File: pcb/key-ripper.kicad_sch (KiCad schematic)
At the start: 193 parts, among them J1 Conn_01x03, SW1 ESC, SW10 F9, SW11 F10, SW12 F11, SW13 F12, SW14 TILDE, SW15 1, SW16 2, SW17 3, SW18 4, SW19 5, SW2 F1, SW20 6, SW21 7, SW22 8, SW23 9, SW24 0, SW25 -, SW26 +, SW27 BACKSPACE, SW28 TAB, SW29 Q, SW3 F2, SW30 W, SW31 E, SW32 R, SW33 T, SW34 Y, SW35 U, SW36 I, SW37 O, SW38 P, SW39 [, SW4 F3, SW40 ], SW41 BACKSLASH, SW42 CAPS, SW43 A, SW44 S, SW45 D, SW46 F, SW47 G, SW48 H, SW49 J, SW5 F4, SW50 K, SW51 L, SW52 ;, SW53 ', SW54 ENTER, SW55 L_SHIFT, SW56 Z, SW57 X, SW58 C, SW59 V, SW6 F5, SW60 B, SW61 N, SW62 M, SW63 ,, SW64 ., SW65 FWD_SLASH, SW66 UP, SW67 FN, SW68 BL_CTRL, SW69 L_ALT, SW7 F6, SW70 L_CMD, SW71 SPACE, SW72 R_CMD, SW73 LEFT, SW74 DOWN, SW75 RIGHT, SW8 F7, SW9 F8, U1 RP2040, U2 TYPE-C-31-M-12, U3 XC6206PxxxMR, U4 W25Q128JVS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

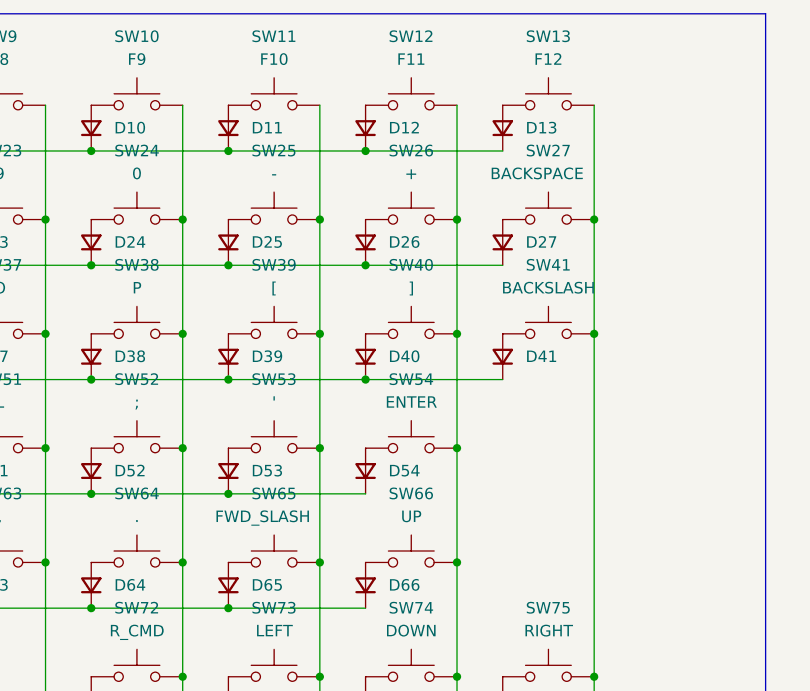
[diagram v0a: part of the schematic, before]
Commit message: Reposition key name silk screens
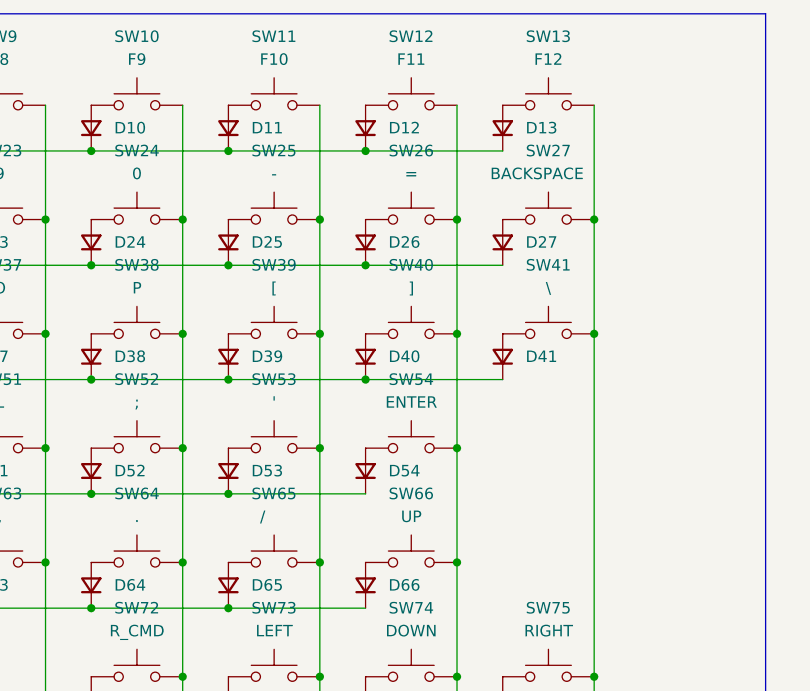
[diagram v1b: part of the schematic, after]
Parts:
- SW26: value + -> =
- SW41: value BACKSLASH -> \
- SW65: value FWD_SLASH -> /
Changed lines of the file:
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@@
     (in_bom yes) (on_board yes) (fields_autoplaced)
     (property "Reference" "SW41" (id 0) (at 229.87 41.91 0))
-    (property "Value" "BACKSLASH" (id 1) (at 229.87 44.45 0))
+    (property "Value" "\\" (id 1) (at 229.87 44.45 0))
     (property "Footprint" "Switch_Keyboard_Hotswap_Kailh:SW_Hotswap_Kailh_MX_1.50u" (id 2) (at 229.87 44.45 0)
       (effects (font (size 1.27 1.27)) hide)
@@
     (in_bom yes) (on_board yes)
     (property "Reference" "SW65" (id 0) (at 199.39 67.31 0))
-    (property "Value" "FWD_SLASH" (id 1) (at 198.12 69.85 0))
+    (property "Value" "/" (id 1) (at 198.12 69.85 0))
     (property "Footprint" "Switch_Keyboard_Hotswap_Kailh:SW_Hotswap_Kailh_MX_1.00u" (id 2) (at 199.39 69.85 0)
       (effects (font (size 1.27 1.27)) hide)
@@
     (in_bom yes) (on_board yes) (fields_autoplaced)
     (property "Reference" "SW26" (id 0) (at 214.63 29.21 0))
-    (property "Value" "+" (id 1) (at 214.63 31.75 0))
+    (property "Value" "=" (id 1) (at 214.63 31.75 0))
     (property "Footprint" "Switch_Keyboard_Hotswap_Kailh:SW_Hotswap_Kailh_MX_1.00u" (id 2) (at 214.63 31.75 0)
       (effects (font (size 1.27 1.27)) hide)
@@
     )
     (path "/aab53e21-b21f-4d92-85bb-8417588d20bc"
-      (reference "SW26") (unit 1) (value "+") (footprint "Switch_Keyboard_Hotswap_Kailh:SW_Hotswap_Kailh_MX_1.00u")
+      (reference "SW26") (unit 1) (value "=") (footprint "Switch_Keyboard_Hotswap_Kailh:SW_Hotswap_Kailh_MX_1.00u")
     )
     (path "/5bb9af28-7152-47d8-b0f0-f72e52c977fa"
@@
     )
     (path "/7a69d6fe-7973-4dc9-9df9-c8dcf9e8b078"
-      (reference "SW41") (unit 1) (value "BACKSLASH") (footprint "Switch_Keyboard_Hotswap_Kailh:SW_Hotswap_Kailh_MX_1.50u")
+      (reference "SW41") (unit 1) (value "\\") (footprint "Switch_Keyboard_Hotswap_Kailh:SW_Hotswap_Kailh_MX_1.50u")
     )
     (path "/e2a1f767-222e-427f-86d9-edbcee5a8109"
@@
     )
     (path "/a2ea1d89-2319-4e89-804e-139e25599a5f"
-      (reference "SW65") (unit 1) (value "FWD_SLASH") (footprint "Switch_Keyboard_Hotswap_Kailh:SW_Hotswap_Kailh_MX_1.00u")
+      (reference "SW65") (unit 1) (value "/") (footprint "Switch_Keyboard_Hotswap_Kailh:SW_Hotswap_Kailh_MX_1.00u")
     )
     (path "/00647e3f-5f42-4695-854e-ff5ad3d6436e"

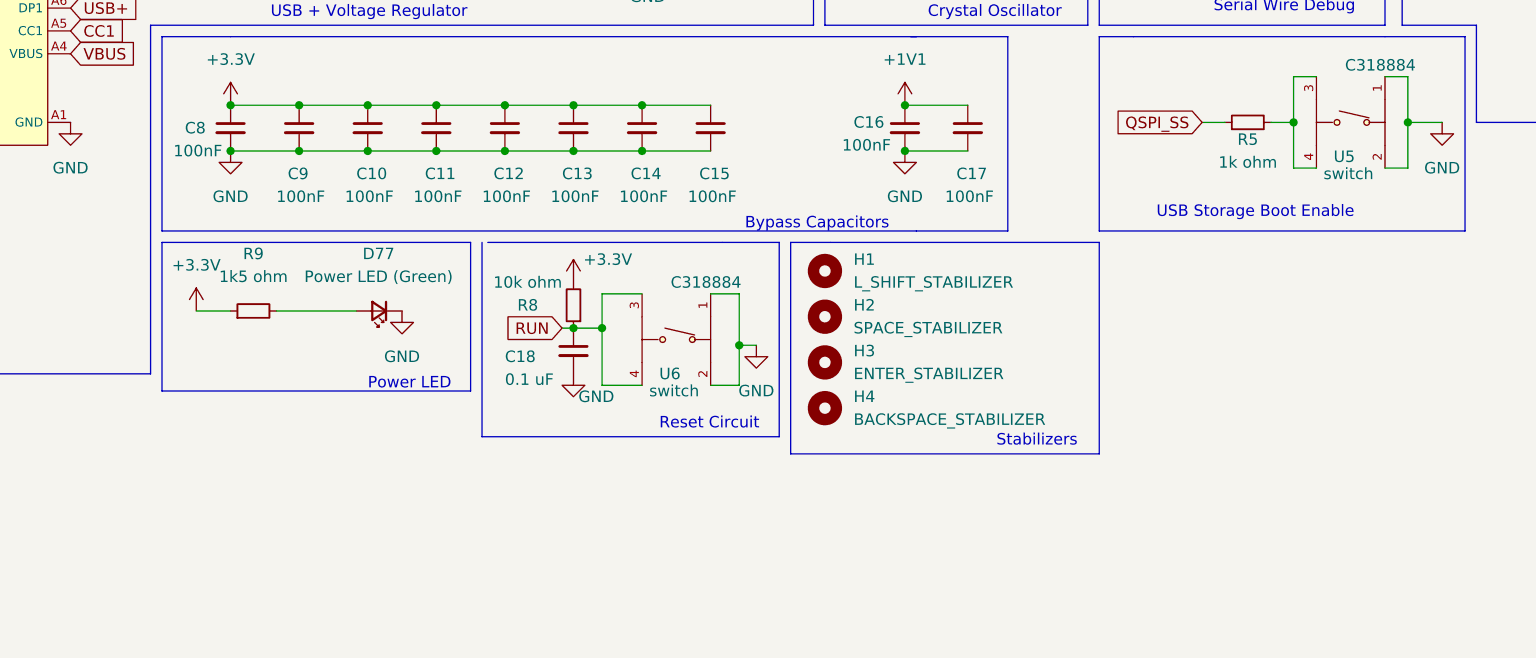
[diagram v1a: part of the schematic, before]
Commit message: Add mounting holes
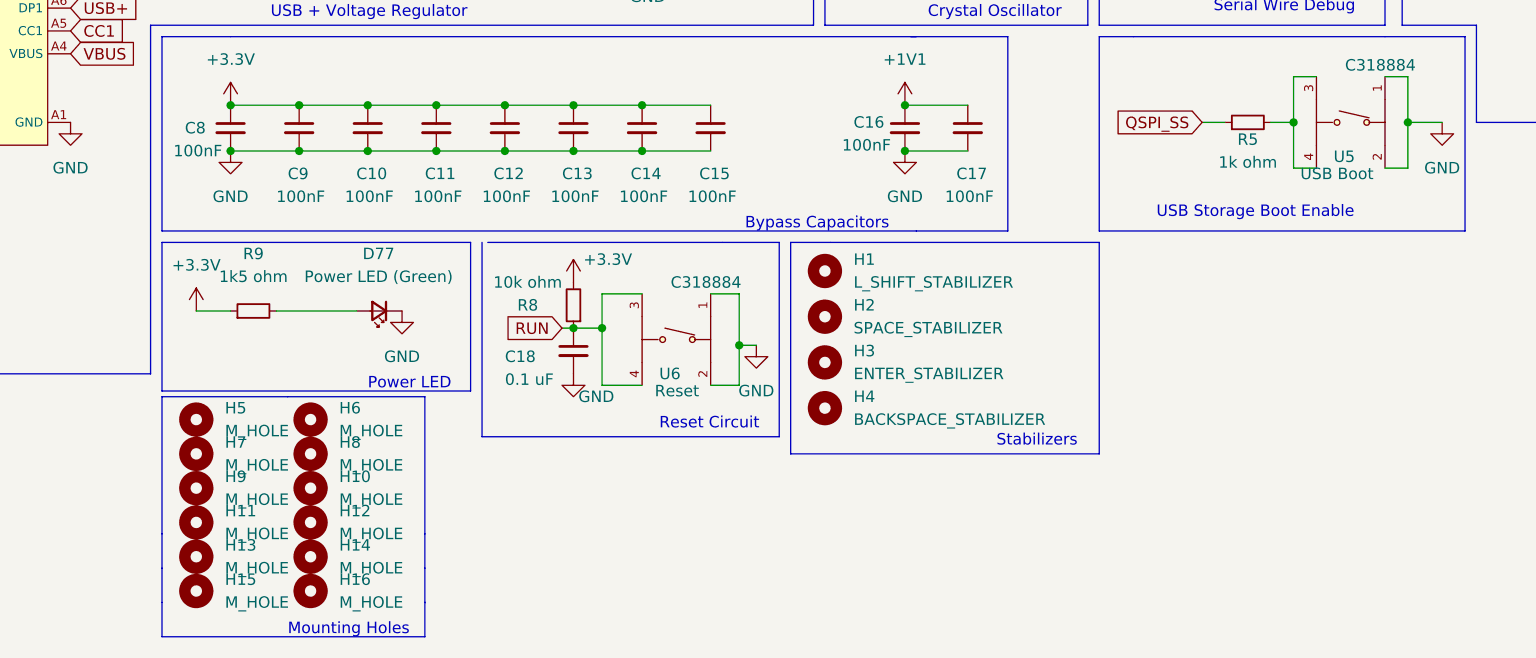
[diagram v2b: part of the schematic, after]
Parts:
- added H10, H11, H12, H13, H14, H15, H16, H5, H6, H7, H8, H9: M_HOLE, MountingHole:MountingHole_2.2mm_M2, symbol Mechanical:MountingHole
- U5: value switch -> USB Boot
- U6: value switch -> Reset
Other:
- note added: "Mounting Holes"

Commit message: Accomodate larger USB termination resistor footprints
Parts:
- R1, R2: footprint Resistor_SMD:R_0402_1005Metric -> Resistor_SMD:R_0603_1608Metric
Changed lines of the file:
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@@
     (property "Reference" "R2" (id 0) (at -4.445 57.785 90))
     (property "Value" "27 ohm" (id 1) (at -4.445 60.325 90))
-    (property "Footprint" "Resistor_SMD:R_0402_1005Metric" (id 2) (at -4.445 55.88 0)
+    (property "Footprint" "Resistor_SMD:R_0603_1608Metric" (id 2) (at -4.445 55.88 0)
       (effects (font (size 1.27 1.27)) hide)
     )
@@
     (property "Reference" "R1" (id 0) (at -4.445 46.99 90))
     (property "Value" "27 ohm" (id 1) (at -4.445 49.53 90))
-    (property "Footprint" "Resistor_SMD:R_0402_1005Metric" (id 2) (at -4.445 53.34 0)
+    (property "Footprint" "Resistor_SMD:R_0603_1608Metric" (id 2) (at -4.445 53.34 0)
       (effects (font (size 1.27 1.27)) hide)
     )
@@
     )
     (path "/79a4d81f-b2a6-46ef-8d14-ab4fe93dbf29"
-      (reference "R1") (unit 1) (value "27 ohm") (footprint "Resistor_SMD:R_0402_1005Metric")
+      (reference "R1") (unit 1) (value "27 ohm") (footprint "Resistor_SMD:R_0603_1608Metric")
     )
     (path "/5c7b105b-3de7-468d-9eb2-3a3b647ae040"
-      (reference "R2") (unit 1) (value "27 ohm") (footprint "Resistor_SMD:R_0402_1005Metric")
+      (reference "R2") (unit 1) (value "27 ohm") (footprint "Resistor_SMD:R_0603_1608Metric")
     )
     (path "/e3a59236-f08b-40ae-bc75-a0d6e7e2a9e2"
